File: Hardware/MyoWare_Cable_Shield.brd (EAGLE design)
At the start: 52.3 x 20.7 mm, 18 parts

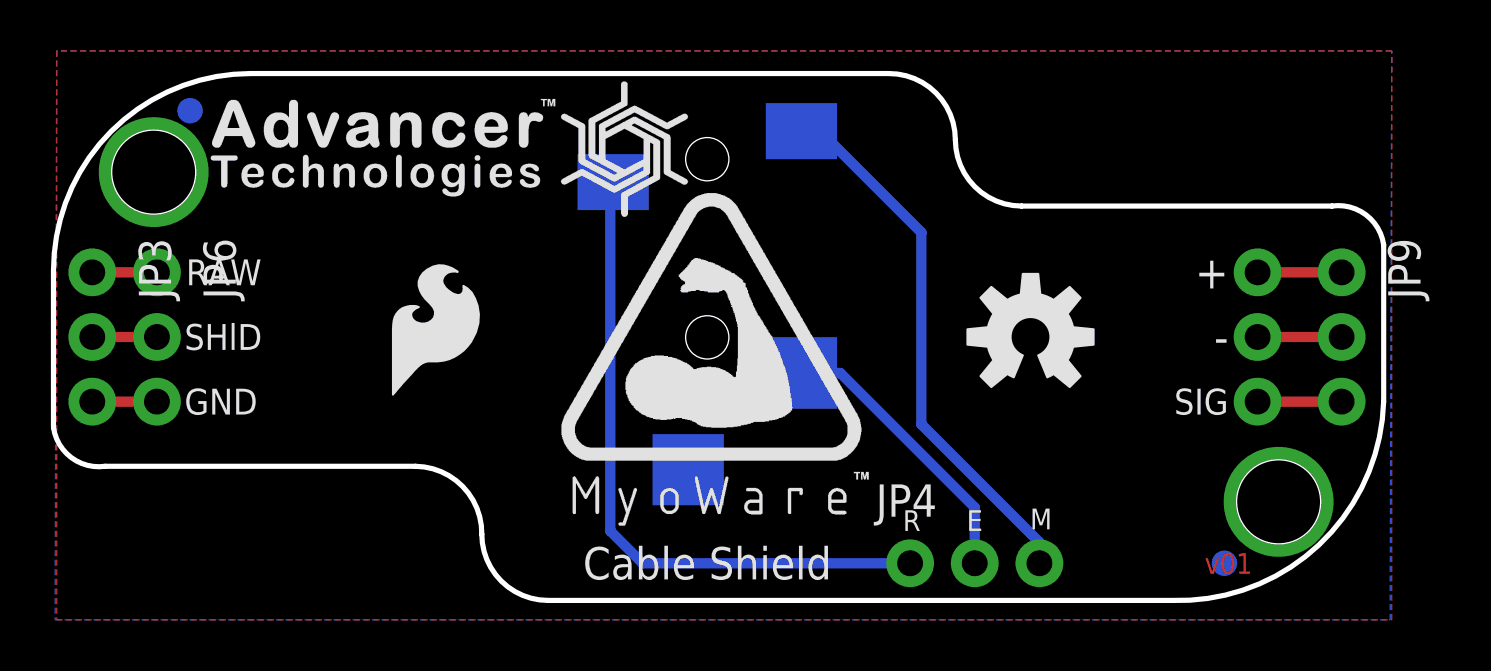
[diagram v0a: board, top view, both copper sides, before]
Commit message: changed audio jack to our common part
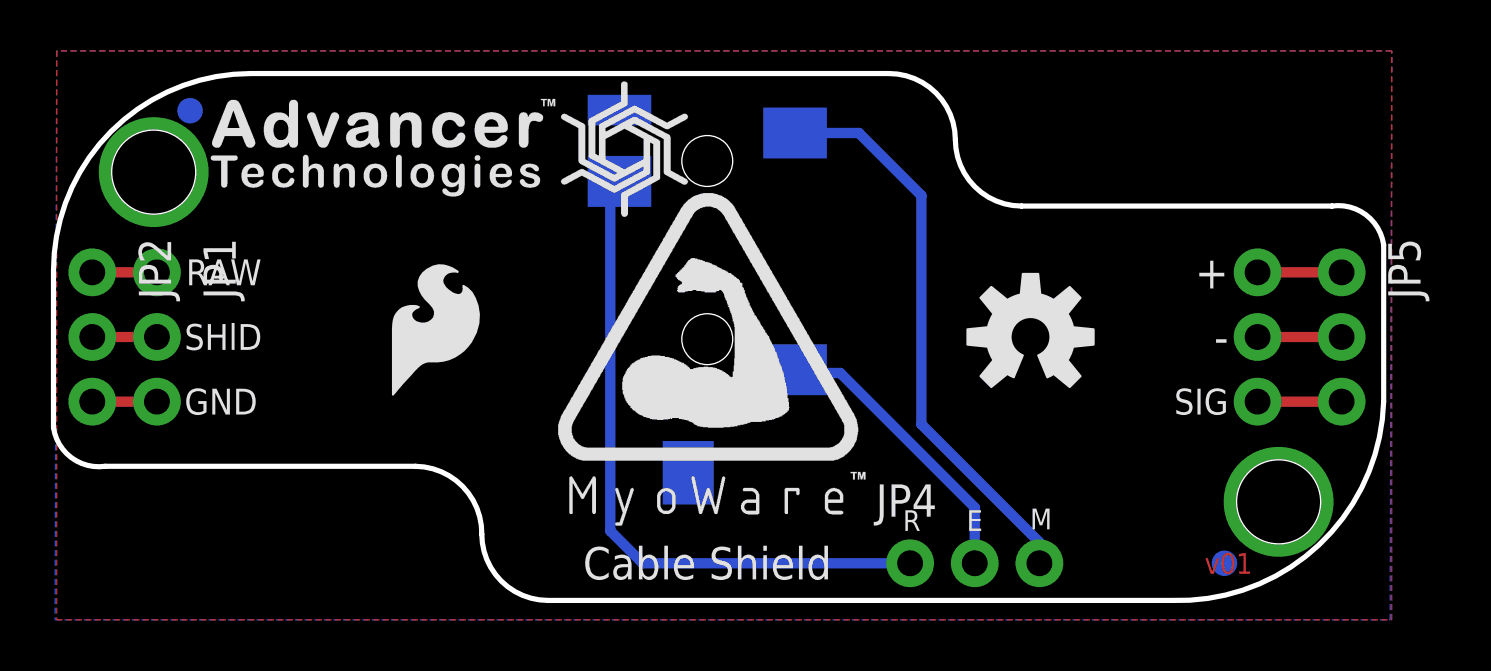
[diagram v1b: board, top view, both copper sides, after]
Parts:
- removed U$1: AUDIO_JACK, advancer-technologies:CUI_3.5MM_AUDIO_JACK
- removed U$4: (no value), advancer-technologies:MYOWARE_LOGO
- added JP1: Power, SparkFun-Connectors:1X03_NO_SILK
- added LOGO: (no value), advancer-technologies:MYOWARE_LOGO
- JP3: value Power -> (none); device SparkFun-Connectors:1X03_NO_SILK -> SparkFun-Connectors:AUDIO-JACK-3.5MM-SMD
- LOGO1: value OSHW-LOGOM -> SFE_LOGO_FLAME.2_INCH; device SparkFun-Aesthetics:OSHW-LOGO-M -> SparkFun-Aesthetics:SFE_LOGO_FLAME_.2
- LOGO2: value SFE_LOGO_FLAME.2_INCH -> OSHW-LOGOM; device SparkFun-Aesthetics:SFE_LOGO_FLAME_.2 -> SparkFun-Aesthetics:OSHW-LOGO-M
- moved JP2 45.8 mm to (-24.2, 2.54)
- moved FID1 44.4 mm to (20.3, -8.89)
- moved FID2 44.4 mm to (-20.3, 8.89)
- moved JP6 43.2 mm to (21.6, 2.54)
- moved LOGO1 25.5 mm to (-12.7, -2.54)
- moved LOGO2 25.5 mm to (12.7, 0.00)
- moved JP3 25.4 mm to (0.00, 10.4), flipped to the bottom
- renumbered JP9 to JP5, U$9 to SPIRAL
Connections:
- net END: now also JP3.TIP; no longer U$1.2
- net GND: now also JP1.3, JP2.3, JP6.2; no longer JP2.2, JP3.3, JP6.3
- net MID: now also JP3.SLEEVE; no longer U$1.1
- net RAW: now also JP1.1, JP2.1; no longer JP3.1, JP6.1
- net SHIELD: now also JP1.2, JP2.2; no longer JP3.2, JP6.2
- net SIG: now also JP6.3; no longer JP2.3
- net VCC: now also JP6.1; no longer JP2.1
- net VREF: now also JP3.RING; no longer U$1.3
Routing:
- net MID: track 21.3 -> 22.3 mm
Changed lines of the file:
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@@
 <layer number="45" name="Holes" color="7" fill="1" visible="yes" active="yes"/>
 <layer number="46" name="Milling" color="3" fill="1" visible="no" active="yes"/>
-<layer number="47" name="Measures" color="7" fill="1" visible="yes" active="yes"/>
+<layer number="47" name="Measures" color="7" fill="1" visible="no" active="yes"/>
 <layer number="48" name="Document" color="7" fill="1" visible="no" active="yes"/>
 <layer number="49" name="Reference" color="3" fill="1" visible="yes" active="yes"/>
@@
 <layer number="113" name="IDFDebug" color="4" fill="1" visible="no" active="yes"/>
 <layer number="116" name="Patch_BOT" color="9" fill="4" visible="no" active="yes"/>
+<layer number="118" name="Rect_Pads" color="7" fill="1" visible="no" active="yes"/>
 <layer number="121" name="_tsilk" color="7" fill="1" visible="no" active="yes"/>
 <layer number="122" name="_bsilk" color="7" fill="1" visible="no" active="yes"/>
@@
 <text x="20.28825" y="-2.54" size="1.016" layer="22" font="vector" ratio="17" rot="MR180" align="center-right">SIG</text>
 <text x="20.28825" y="0" size="1.27" layer="22" font="vector" ratio="17" rot="MR180" align="center-right">-</text>
-<dimension x1="22.44725" y1="-6.477" x2="-21.74875" y2="6.477" x3="0.34925" y3="11.43" textsize="1.778" textratio="15" layer="47" dtype="horizontal" unit="inch"/>
-<dimension x1="-25.68575" y1="-3.556" x2="26.5557" y2="-3.556" x3="0.434975" y3="15.6972" textsize="1.778" textratio="15" layer="47" unit="inch"/>
+<dimension x1="22.44725" y1="-6.477" x2="-21.74875" y2="6.477" x3="0.34925" y3="13.97" textsize="1.778" textratio="15" layer="47" dtype="horizontal" unit="inch"/>
+<dimension x1="-25.68575" y1="-3.556" x2="26.5557" y2="-3.556" x3="0.434975" y3="18.2372" textsize="1.778" textratio="15" layer="47" unit="inch"/>
 <dimension x1="22.44725" y1="-6.477" x2="-21.74875" y2="6.477" x3="-27.9908" y3="0" textsize="1.778" textratio="15" layer="47" dtype="vertical" unit="inch"/>
 <dimension x1="-17.93875" y1="10.3505" x2="-5.1943" y2="-10.3505" x3="-33.1597" y3="0" textsize="1.778" textratio="15" layer="47" dtype="vertical" unit="inch"/>
-<text x="0" y="20.32" size="1.778" layer="47" font="vector" ratio="15" align="center">All units in inches</text>
+<text x="0" y="22.86" size="1.778" layer="47" font="vector" ratio="15" align="center">All units in inches</text>
 <text x="-20.66925" y="2.54" size="1.016" layer="22" font="vector" ratio="17" rot="MR0" align="center-right">RAW</text>
 <text x="-20.60575" y="0" size="1.016" layer="22" font="vector" ratio="17" rot="MR0" align="center-right">SHlD</text>
@@
 <element name="U$6" library="advancer-technologies" package="ADVANCER_LOGO" value="" x="-13.08735" y="7.2263"/>
 <element name="U$3" library="advancer-technologies" package="ROHS" value="" x="-9.55675" y="-1.8415" smashed="yes" rot="MR0"/>
-<element name="JP2" library="SparkFun-Connectors" package="1X03_NO_SILK" value="Power" x="21.62175" y="2.54" smashed="yes" rot="R270"/>
-<element name="U$4" library="advancer-technologies" package="MYOWARE_LOGO" value="" x="0.127" y="-0.889"/>
-<element name="U$9" library="advancer-technologies" package="SPIRAL_LOGO_60%" value="" x="-3.2131" y="7.3787"/>
+<element name="JP6" library="SparkFun-Connectors" package="1X03_NO_SILK" value="Power" x="21.62175" y="2.54" smashed="yes" rot="R270"/>
+<element name="LOGO" library="advancer-technologies" package="MYOWARE_LOGO" value="" x="0" y="-0.889"/>
+<element name="SPIRAL" library="advancer-technologies" package="SPIRAL_LOGO_60%" value="" x="-3.2131" y="7.3787"/>
 <element name="JP4" library="SparkFun-Connectors" package="1X03_NO_SILK" value="Power" x="7.96925" y="-8.89"/>
-<element name="JP9" library="SparkFun-Connectors" package="1X03_NO_SILK" value="Power" x="24.92375" y="2.54" rot="R270"/>
-<element name="U$1" library="advancer-technologies" package="CUI_3.5MM_AUDIO_JACK" value="AUDIO_JACK" x="0" y="6.985" rot="MR270"/>
-<element name="JP3" library="SparkFun-Connectors" package="1X03_NO_SILK" value="Power" x="-24.16175" y="2.54" rot="R270"/>
-<element name="JP6" library="SparkFun-Connectors" package="1X03_NO_SILK" value="Power" x="-21.62175" y="2.54" rot="R270"/>
+<element name="JP5" library="SparkFun-Connectors" package="1X03_NO_SILK" value="Power" x="24.92375" y="2.54" rot="R270"/>
+<element name="JP2" library="SparkFun-Connectors" package="1X03_NO_SILK" value="Power" x="-24.16175" y="2.54" rot="R270"/>
+<element name="JP1" library="SparkFun-Connectors" package="1X03_NO_SILK" value="Power" x="-21.62175" y="2.54" rot="R270"/>
 <element name="FRAME1" library="SparkFun-Aesthetics" package="CREATIVE_COMMONS" value="FRAME-LETTER" x="-31.75" y="-25.4"/>
-<element name="LOGO1" library="SparkFun-Aesthetics" package="OSHW-LOGO-M" value="OSHW-LOGOM" x="12.7" y="0"/>
-<element name="LOGO2" library="SparkFun-Aesthetics" package="SFE_LOGO_FLAME_.2" value="SFE_LOGO_FLAME.2_INCH" x="-12.7" y="-2.54"/>
+<element name="LOGO2" library="SparkFun-Aesthetics" package="OSHW-LOGO-M" value="OSHW-LOGOM" x="12.7" y="0"/>
+<element name="LOGO1" library="SparkFun-Aesthetics" package="SFE_LOGO_FLAME_.2" value="SFE_LOGO_FLAME.2_INCH" x="-12.7" y="-2.54"/>
 <element name="STANDOFF1" library="SparkFun-Electromechanical" package="STAND-OFF" value="STAND-OFF" x="-21.74875" y="6.477"/>
 <element name="STANDOFF2" library="SparkFun-Electromechanical" package="STAND-OFF" value="STAND-OFF" x="22.44725" y="-6.477"/>
-<element name="FID1" library="SparkFun-Aesthetics" package="FIDUCIAL-1X2" value="FIDUCIAL1X2" x="-20.32" y="8.89" rot="MR0"/>
-<element name="FID2" library="SparkFun-Aesthetics" package="FIDUCIAL-1X2" value="FIDUCIAL1X2" x="20.32" y="-8.89" rot="MR0"/>
+<element name="FID2" library="SparkFun-Aesthetics" package="FIDUCIAL-1X2" value="FIDUCIAL1X2" x="-20.32" y="8.89" rot="MR0"/>
+<element name="FID1" library="SparkFun-Aesthetics" package="FIDUCIAL-1X2" value="FIDUCIAL1X2" x="20.32" y="-8.89" rot="MR0"/>
+<element name="JP3" library="SparkFun-Connectors" package="AUDIO-JACK-3.5MM-SMD" value="" x="0" y="10.414" rot="MR270">
+<attribute name="PROD_ID" value="CONN-10353" x="0" y="10.414" size="1.778" layer="28" rot="MR270" display="off"/>
+</element>
 </elements>
 <signals>
 <signal name="SHIELD">
-<contactref element="JP3" pad="2"/>
-<contactref element="JP6" pad="2"/>
+<contactref element="JP2" pad="2"/>
+<contactref element="JP1" pad="2"/>
 <wire x1="-24.16175" y1="0" x2="-21.62175" y2="0" width="0.4064" layer="1"/>
 </signal>
 <signal name="RAW">
-<contactref element="JP3" pad="1"/>
-<contactref element="JP6" pad="1"/>
+<contactref element="JP2" pad="1"/>
+<contactref element="JP1" pad="1"/>
 <wire x1="-24.16175" y1="2.54" x2="-21.62175" y2="2.54" width="0.4064" layer="1"/>
 </signal>
 <signal name="MID">
-<contactref element="U$1" pad="1"/>
 <contactref element="JP4" pad="3"/>
-<wire x1="8.41375" y1="4.1015" x2="8.41375" y2="-3.429" width="0.4064" layer="16"/>
+<wire x1="8.41375" y1="5.55625" x2="8.41375" y2="-3.429" width="0.4064" layer="16"/>
 <wire x1="8.41375" y1="-3.429" x2="13.04925" y2="-8.0645" width="0.4064" layer="16"/>
 <wire x1="13.04925" y1="-8.0645" x2="13.04925" y2="-8.89" width="0.4064" layer="16"/>
-<wire x1="8.41375" y1="4.1015" x2="4.43025" y2="8.085" width="0.4064" layer="16"/>
-<wire x1="4.43025" y1="8.085" x2="3.7" y2="8.085" width="0.4064" layer="16"/>
+<contactref element="JP3" pad="SLEEVE"/>
+<wire x1="3.45" y1="8.014" x2="5.956" y2="8.014" width="0.4064" layer="16"/>
+<wire x1="5.956" y1="8.014" x2="8.41375" y2="5.55625" width="0.4064" layer="16"/>
 </signal>
 <signal name="END">
-<contactref element="U$1" pad="2"/>
 <contactref element="JP4" pad="2"/>
 <wire x1="10.50925" y1="-8.89" x2="10.50925" y2="-6.69925" width="0.4064" layer="16"/>
 <wire x1="10.50925" y1="-6.69925" x2="5.225" y2="-1.415" width="0.4064" layer="16"/>
-<wire x1="5.225" y1="-1.415" x2="3.7" y2="-1.415" width="0.4064" layer="16"/>
+<contactref element="JP3" pad="TIP"/>
+<wire x1="5.225" y1="-1.415" x2="3.45" y2="-1.415" width="0.4064" layer="16"/>
+<wire x1="3.45" y1="-1.415" x2="3.45" y2="-1.286" width="0.4064" layer="16"/>
 </signal>
 <signal name="VREF">
-<contactref element="U$1" pad="3"/>
 <contactref element="JP4" pad="1"/>
 <wire x1="7.96925" y1="-8.89" x2="-2.54" y2="-8.89" width="0.4064" layer="16"/>
 <wire x1="-2.54" y1="-8.89" x2="-3.81" y2="-7.62" width="0.4064" layer="16"/>
 <wire x1="-3.81" y1="-7.62" x2="-3.81" y2="5.975" width="0.4064" layer="16"/>
-<wire x1="-3.81" y1="5.975" x2="-3.7" y2="6.085" width="0.4064" layer="16"/>
+<contactref element="JP3" pad="RING"/>
+<wire x1="-3.81" y1="5.975" x2="-3.671" y2="6.114" width="0.4064" layer="16"/>
+<wire x1="-3.671" y1="6.114" x2="-3.45" y2="6.114" width="0.4064" layer="16"/>
 </signal>
 <signal name="SIG">
-<contactref element="JP2" pad="3"/>
-<contactref element="JP9" pad="3"/>
+<contactref element="JP6" pad="3"/>
+<contactref element="JP5" pad="3"/>
 <wire x1="21.62175" y1="-2.54" x2="24.92375" y2="-2.54" width="0.4064" layer="1"/>
 </signal>
@@
 <vertex x="-25.55875" y="11.2395"/>
 </polygon>
-<contactref element="JP2" pad="2"/>
-<contactref element="JP9" pad="2"/>
+<contactref element="JP6" pad="2"/>
+<contactref element="JP5" pad="2"/>
 <wire x1="21.62175" y1="0" x2="24.92375" y2="0" width="0.4064" layer="1"/>
-<contactref element="JP3" pad="3"/>
-<contactref element="JP6" pad="3"/>
+<contactref element="JP2" pad="3"/>
+<contactref element="JP1" pad="3"/>
 <wire x1="-24.16175" y1="-2.54" x2="-21.62175" y2="-2.54" width="0.4064" layer="1"/>
 </signal>
@@
 </signal>
 <signal name="VCC">
-<contactref element="JP9" pad="1"/>
-<contactref element="JP2" pad="1"/>
+<contactref element="JP5" pad="1"/>
+<contactref element="JP6" pad="1"/>
 <wire x1="21.62175" y1="2.54" x2="24.92375" y2="2.54" width="0.4064" layer="1"/>
 </signal>

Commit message: Added cam friendlier versions of the RoSH and PB Free images
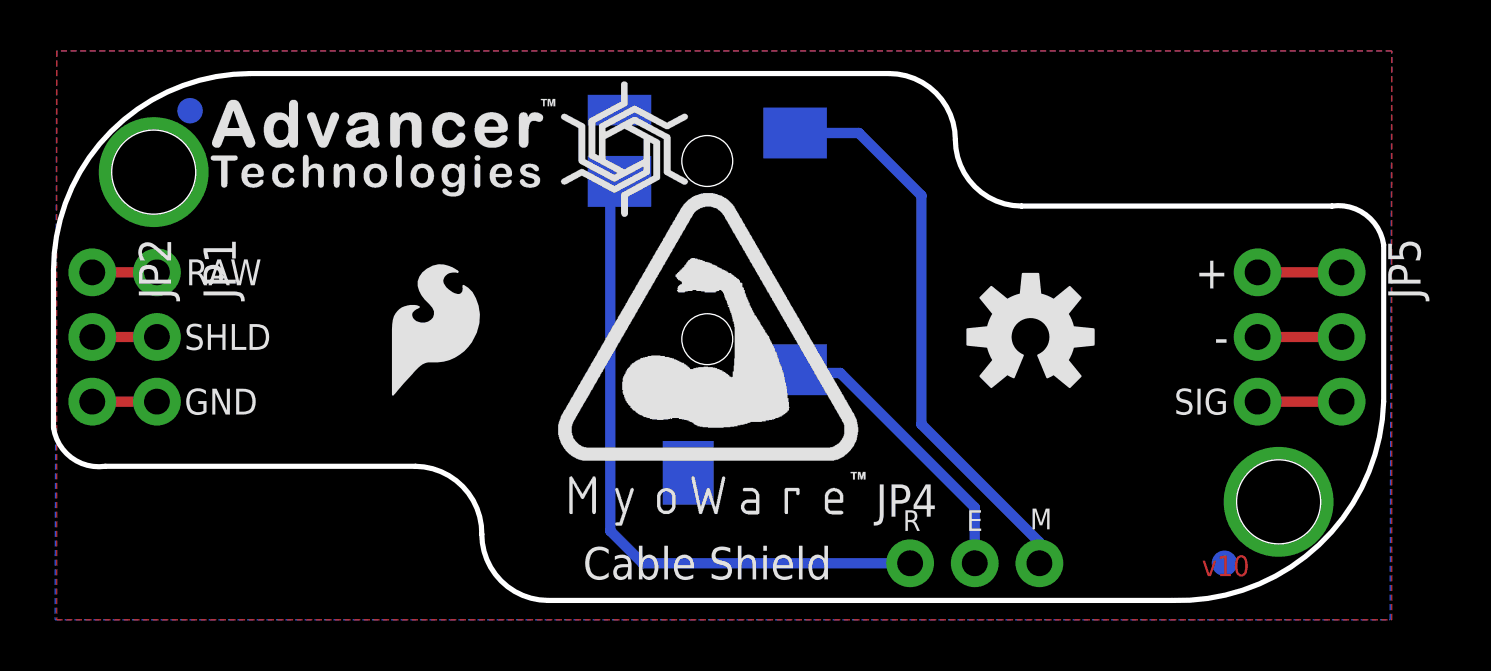
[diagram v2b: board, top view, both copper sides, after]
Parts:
- U$3: device advancer-technologies:ROHS -> SparkFun-Aesthetics:ROHS_LOGO_0.18_IN
- U$5: device advancer-technologies:PB-FREE -> SparkFun-Aesthetics:NO_PB_LOGO_0.120
- moved U$5 0.74 mm to (14.4, -1.91)
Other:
- board text added: "SHLD"
- board text added: "v10"
- board text removed: "SHlD"
- board text removed: "v01"
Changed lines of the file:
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@@
 <?xml version="1.0" encoding="utf-8"?>
 <!DOCTYPE eagle SYSTEM "eagle.dtd">
-<eagle version="7.3.1">
+<eagle version="7.3.0">
 <drawing>
 <settings>
@@
 <layer number="47" name="Measures" color="7" fill="1" visible="no" active="yes"/>
 <layer number="48" name="Document" color="7" fill="1" visible="no" active="yes"/>
-<layer number="49" name="Reference" color="3" fill="1" visible="yes" active="yes"/>
+<layer number="49" name="Reference" color="3" fill="1" visible="no" active="yes"/>
 <layer number="50" name="dxf" color="7" fill="1" visible="no" active="yes"/>
 <layer number="51" name="tDocu" color="6" fill="1" visible="yes" active="yes"/>
@@
 <text x="10.50925" y="-7.62" size="0.8128" layer="21" font="vector" ratio="20" align="bottom-center">E</text>
 <text x="-20.47875" y="2.54" size="1.016" layer="21" font="vector" ratio="17" align="center-left">RAW</text>
-<text x="-20.54225" y="0" size="1.016" layer="21" font="vector" ratio="17" align="center-left">SHlD</text>
+<text x="-20.54225" y="0" size="1.016" layer="21" font="vector" ratio="17" align="center-left">SHLD</text>
 <wire x1="26.57475" y1="3.6195" x2="26.57475" y2="-2.54" width="0.2032" layer="20"/>
 <wire x1="26.57475" y1="3.6195" x2="24.54275" y2="5.1435" width="0.2032" layer="20" curve="90"/>
@@
 <text x="-1.27" y="-25.4" size="1.778" layer="51" font="vector">Brian E Kaminski of Advancer Technologies</text>
 <text x="-20.32" y="-27.94" size="1.778" layer="51" font="vector">Revised by: Brent Wilkins</text>
-<text x="19.544" y="-9.303" size="0.8128" layer="1" font="vector" ratio="20">v01</text>
+<text x="19.431" y="-9.398" size="0.8128" layer="1" font="vector" ratio="20">v10</text>
 <text x="20.28825" y="2.54" size="1.27" layer="22" font="vector" ratio="20" rot="MR180" align="center-right">+</text>
 <text x="20.28825" y="-2.54" size="1.016" layer="22" font="vector" ratio="17" rot="MR180" align="center-right">SIG</text>
@@
 <text x="0" y="22.86" size="1.778" layer="47" font="vector" ratio="15" align="center">All units in inches</text>
 <text x="-20.66925" y="2.54" size="1.016" layer="22" font="vector" ratio="17" rot="MR0" align="center-right">RAW</text>
-<text x="-20.60575" y="0" size="1.016" layer="22" font="vector" ratio="17" rot="MR0" align="center-right">SHlD</text>
+<text x="-20.60575" y="0" size="1.016" layer="22" font="vector" ratio="17" rot="MR0" align="center-right">SHLD</text>
 <text x="-20.60575" y="-2.54" size="1.016" layer="22" font="vector" ratio="17" rot="MR0" align="center-right">GND</text>
 <text x="12.92225" y="-7.5565" size="0.8128" layer="22" font="vector" ratio="20" rot="MR0" align="bottom-center">M</text>
@@
 </autorouter>
 <elements>
-<element name="U$5" library="advancer-technologies" package="PB-FREE" value="" x="15.04315" y="-2.286" rot="MR0"/>
+<element name="U$5" library="SparkFun-Aesthetics" package="NO_PB_LOGO_0.120" value="" x="14.40815" y="-1.905" rot="MR0"/>
 <element name="U$6" library="advancer-technologies" package="ADVANCER_LOGO" value="" x="-13.08735" y="7.2263"/>
-<element name="U$3" library="advancer-technologies" package="ROHS" value="" x="-9.55675" y="-1.8415" smashed="yes" rot="MR0"/>
+<element name="U$3" library="SparkFun-Aesthetics" package="ROHS_LOGO_0.18_IN" value="" x="-9.55675" y="-1.8415" smashed="yes" rot="MR0"/>
 <element name="JP6" library="SparkFun-Connectors" package="1X03_NO_SILK" value="Power" x="21.62175" y="2.54" smashed="yes" rot="R270"/>
 <element name="LOGO" library="advancer-technologies" package="MYOWARE_LOGO" value="" x="0" y="-0.889"/>

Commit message: Gave the jack a value of '3.5mm jack'
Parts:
- JP3: value (none) -> 3.5mm Jack
